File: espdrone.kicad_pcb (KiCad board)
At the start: 6 copper layers, 60 x 60 mm, 503 parts, among them J10 Conn_01x04, J11 Conn_01x04, J12 Conn_01x04, J4 Conn_01x06, J5 Conn_Coaxial, J6 Conn_01x06, J7 Conn_01x06, J8 Conn_01x04, J9 Conn_01x04, Q1 NMOS, Q10 NMOS, Q11 NMOS, Q12 NMOS, Q13 NMOS, Q14 NMOS, Q15 NMOS, Q16 NMOS, Q17 NMOS, Q18 NMOS, Q19 NMOS, Q2 NMOS, Q20 NMOS, Q21 NMOS, Q22 NMOS, Q23 NMOS, Q24 NMOS, Q25 NMOS, Q26 NMOS, Q27 NMOS, Q28 NMOS, Q3 NMOS, Q4 NMOS, Q5 NMOS, Q6 NMOS, Q7 NMOS, Q8 NMOS, Q9 NMOS, U10 FPC-1.0FX-15PWCR-H20, U11 VL53L1CXV0FY1, U12 LIS2MDL, U13 LSM6DS3, U14 PMW3901MB-TXQT_C43496881, U15 STM32G071K8U6, U16 DRV8328ARUYR, U18 STM32G071K8U6, U19 DRV8328ARUYR, U2 USBLC6-2P6, U20 INA180A2, U21 STM32G071K8U6, U22 DRV8328ARUYR, U23 INA180A2, U24 STM32G071K8U6, U25 DRV8328ARUYR, U26 INA180A2, U27 INA190A3IDCKR, U28 INA190A3IDCKR, U29 INA190A3IDCKR, U3 W25Q128JVP, U4 ESP32-C5HF4, U5 LFD182G45DCHD277, U6 TLV62569DBV, U7 INA190A3IDCKR, U8 TPS63070RNMR, U9 TPS2121RUXR, Y1 Crystal_GND24, Y2 Crystal_GND24

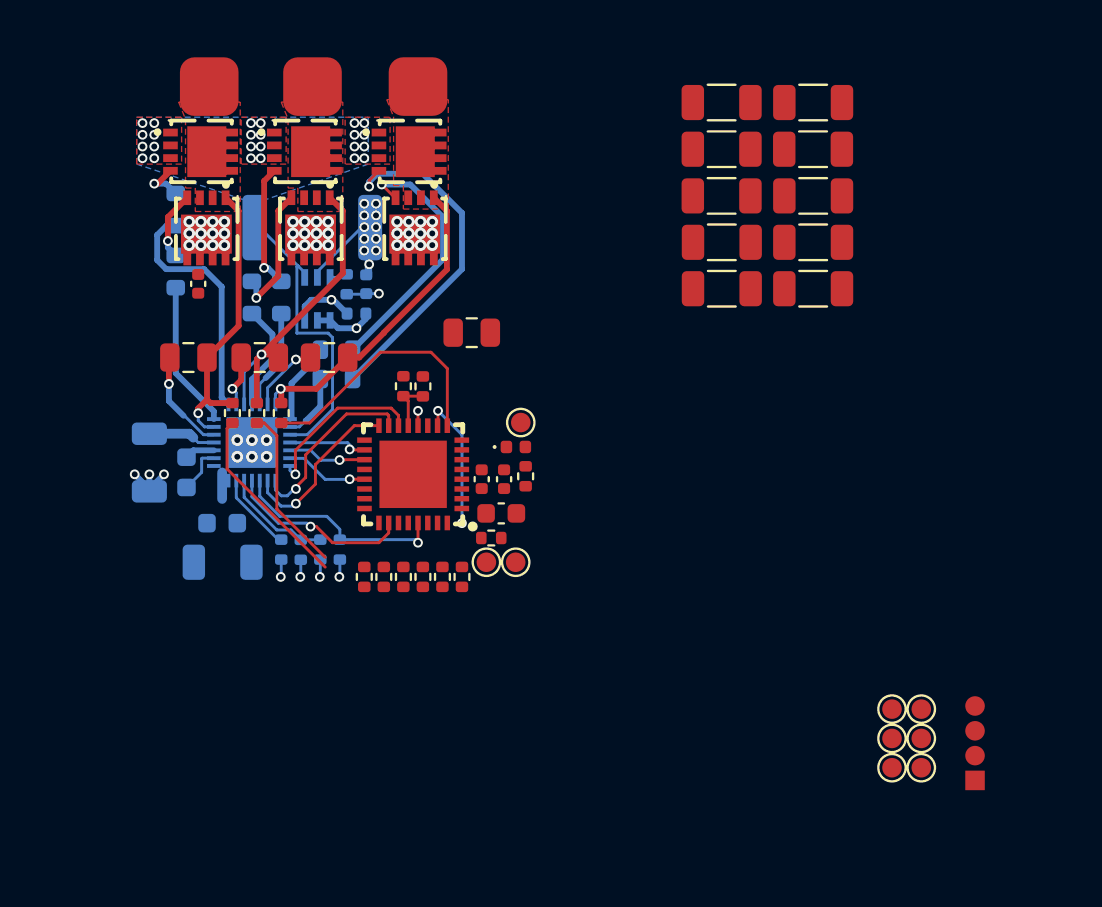
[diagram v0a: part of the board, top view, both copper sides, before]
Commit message: Ostensibly finish ESC routing
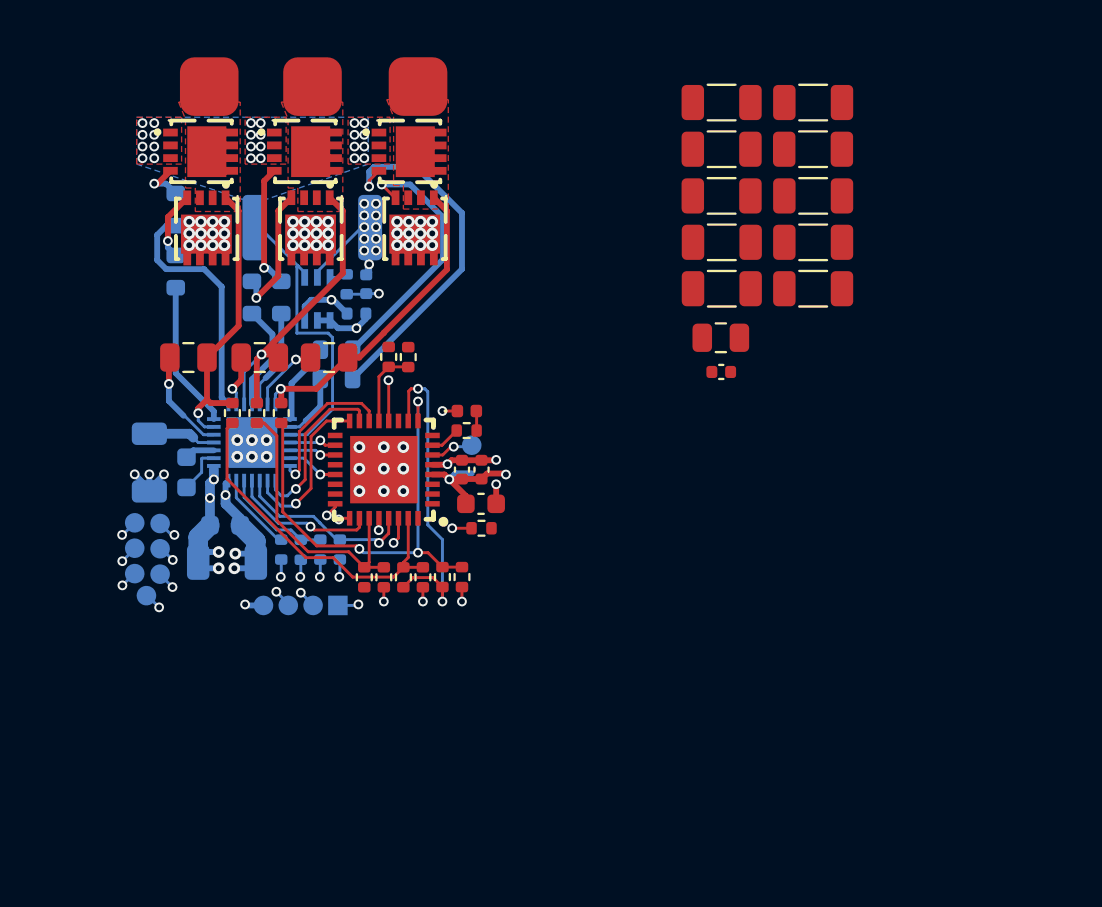
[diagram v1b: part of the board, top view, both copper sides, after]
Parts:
- removed TP19: TestPoint, easyeda2kicad:TestPoint_Pad_D1.0mm_No_Courtyard
- J8, TP11, TP12, TP13, TP14, TP15, TP16, TP17, TP18: moved to B.Cu
- moved TP11 40.2 mm to (116.3, 83.1)
- moved TP12 40.2 mm to (116.3, 81.8)
- moved TP13 40.1 mm to (116.3, 80.5)
- moved TP14 40.0 mm to (115.0, 83.1), turned to 0 degrees
- moved TP15 40.0 mm to (115.0, 81.8), turned to 0 degrees
- moved TP16 39.9 mm to (115.0, 80.5), turned to 0 degrees
- moved J8 33.7 mm to (123.4, 82.5), turned to 0 degrees
- moved C112 27.1 mm to (145.0, 72.8), turned to 180 degrees
- moved TP18 17.5 mm to (115.6, 84.2), turned to 90 degrees
- moved C115 12.8 mm to (145.0, 71.0)
- moved R61 3.82 mm to (132.0, 75.8), turned to 0 degrees
- moved D11 3.11 mm to (132.0, 74.8)
- moved TP17 2.77 mm to (132.2, 76.5), turned to 0 degrees
- moved R75 2.00 mm to (128.8, 83.3)
- moved R76 2.00 mm to (129.8, 83.3)
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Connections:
- TP31 pad 1: /Motors/ESC2/TELEMETRY -> TELEMETRY
- TP43 pad 1: /Motors/ESC3/TELEMETRY -> TELEMETRY
- TP55 pad 1: /Motors/ESC4/TELEMETRY -> TELEMETRY
- U1 pad 6: unconnected-(U1-GPIO6-Pad6) -> TELEMETRY
- U15 pad 30: /Motors/ESC1/TELEMETRY -> TELEMETRY
- U18 pad 30: /Motors/ESC2/TELEMETRY -> TELEMETRY
- U21 pad 30: /Motors/ESC3/TELEMETRY -> TELEMETRY
- U24 pad 30: /Motors/ESC4/TELEMETRY -> TELEMETRY
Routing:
- net GND: track 15.3 -> 31.1 mm, vias 23 -> 43
- net /Motors/ESC1/A_HIGH: track 4.26 -> 17.5 mm, vias 1 -> 2
- net /Motors/ESC1/B_HIGH: track 4.04 -> 15.7 mm, vias 1 -> 2
- net /Motors/ESC1/C_HIGH: track 3.97 -> 15.5 mm, vias 1 -> 2
- net /Motors/ESC1/VSENSE_C: track 13.3 -> 23.7 mm, vias 0 -> 3
- net /Motors/ESC1/VSENSE_REF: track 7.09 -> 16.8 mm
- net /Motors/ESC1/A_LOW: track 8.89 -> 18.1 mm, vias 1 -> 2
- net /Motors/ESC1/NSLEEP: track 9.52 -> 17.9 mm, vias 1 -> 2
- net /Motors/ESC1/VSENSE_A: track 9.57 -> 17.9 mm
- net /Motors/ESC1/B_LOW: track 9.47 -> 17.5 mm, vias 1 -> 2
- net +3V3: track 5.53 -> 13.4 mm, vias 3 -> 6
- net /Motors/ESC1/C_LOW: track 8.67 -> 16.2 mm, vias 1 -> 2
- net /Motors/ESC1/SWDIO: track 0.00 -> 6.78 mm, vias 0 -> 2
- net +BATT: track 1.47 -> 8.12 mm, vias 36 -> 40
- net /Motors/ESC1/VSENSE_B: track 8.55 -> 14.7 mm
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
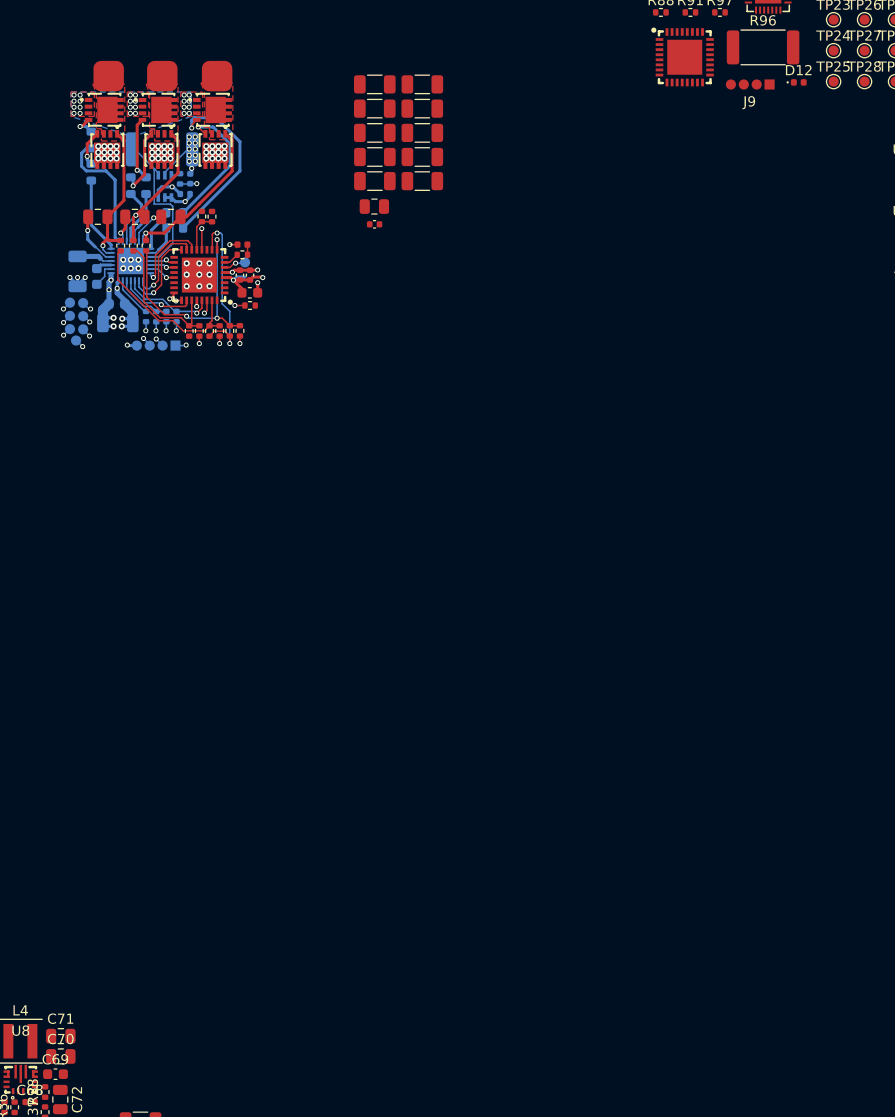
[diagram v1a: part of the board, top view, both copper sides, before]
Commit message: Add dimensions for MOSFET rearranging
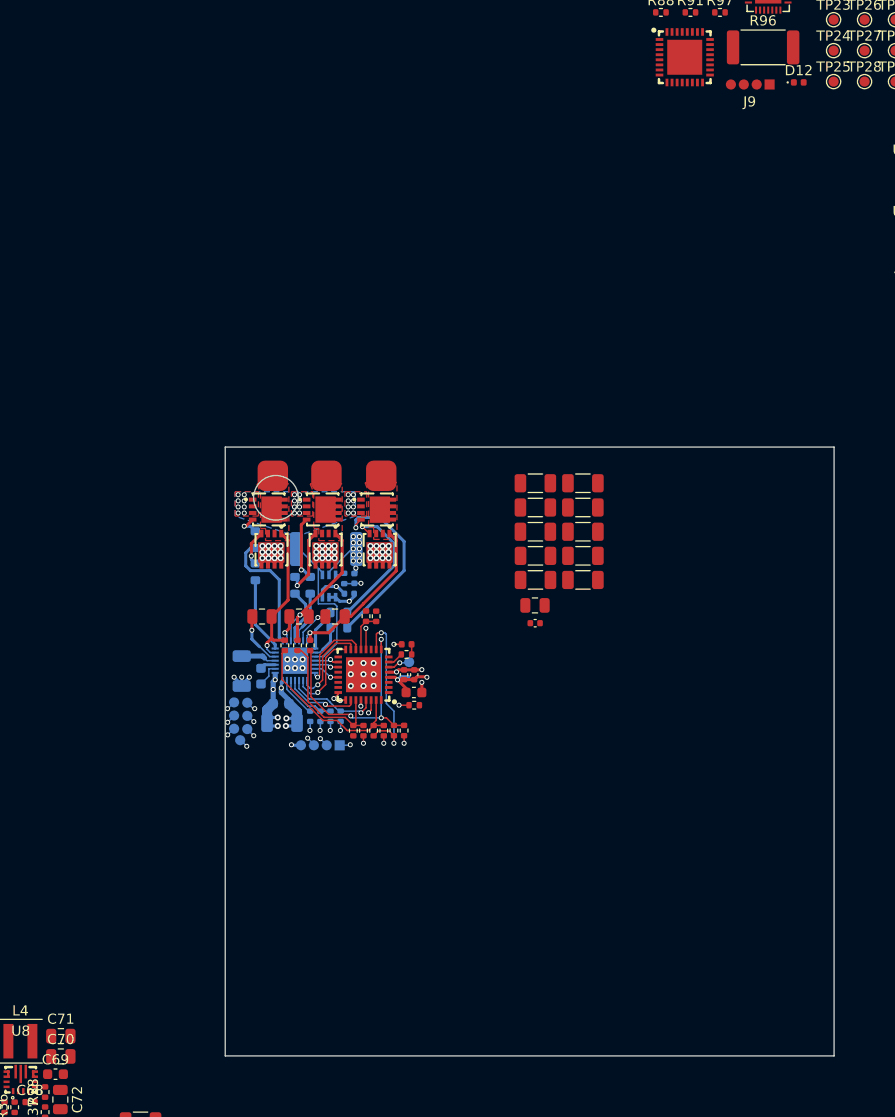
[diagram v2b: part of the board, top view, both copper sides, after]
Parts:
- moved C102 42.6 mm to (135.9, 121.9)
- moved C103 42.6 mm to (135.8, 120.0)
- moved C104 42.6 mm to (148.9, 117.1)
- moved C105 42.6 mm to (131.9, 116.8)
- moved C106 42.6 mm to (147.9, 117.1)
- moved C108 42.6 mm to (148.9, 118.9)
- moved C109 42.6 mm to (133.9, 111.4)
- moved C111 42.6 mm to (141.1, 111.4)
- moved C117 42.6 mm to (142.5, 109.2)
- moved C119 42.6 mm to (143.0, 107.7)
- moved D11 42.6 mm to (148.2, 114.1)
- moved J8 42.6 mm to (139.6, 121.9)
- moved Q7 42.6 mm to (140.2, 104.8)
- moved Q8 42.6 mm to (139.9, 100.9)
- moved R62 42.6 mm to (141.7, 121.2)
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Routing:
- net /Motors/ESC1/B_HIGH: track 15.7 -> 3.34 mm
- net +BATT: track 8.12 -> 20.3 mm
- net GND: track 31.1 -> 35.6 mm
- net /Motors/ESC1/SWCLK: track 6.04 -> 1.49 mm
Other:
- board size 60 x 60 mm -> 167.9 x 121.5 mm

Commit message: Minor ESC adjustments
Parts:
- moved C122 5.53 mm to (155.5, 97.0)
- moved C124 5.53 mm to (155.5, 101.8)
- moved C125 5.53 mm to (155.5, 99.4)
- moved C116 5.53 mm to (155.5, 106.5)
- moved C123 5.53 mm to (155.5, 104.2)
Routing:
- net +BATT: track 20.3 -> 8.12 mm
- net /Motors/ESC1/B_HIGH: track 3.34 -> 13.9 mm
- net GND: track 35.6 -> 31.1 mm
- net /Motors/ESC1/SWCLK: track 1.49 -> 6.04 mm
- net /Motors/ESC1/A_HIGH: track 17.5 -> 14.8 mm
- net /Motors/ESC1/C_HIGH: track 15.7 -> 13.7 mm
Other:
- outline, holes or cut-outs redrawn

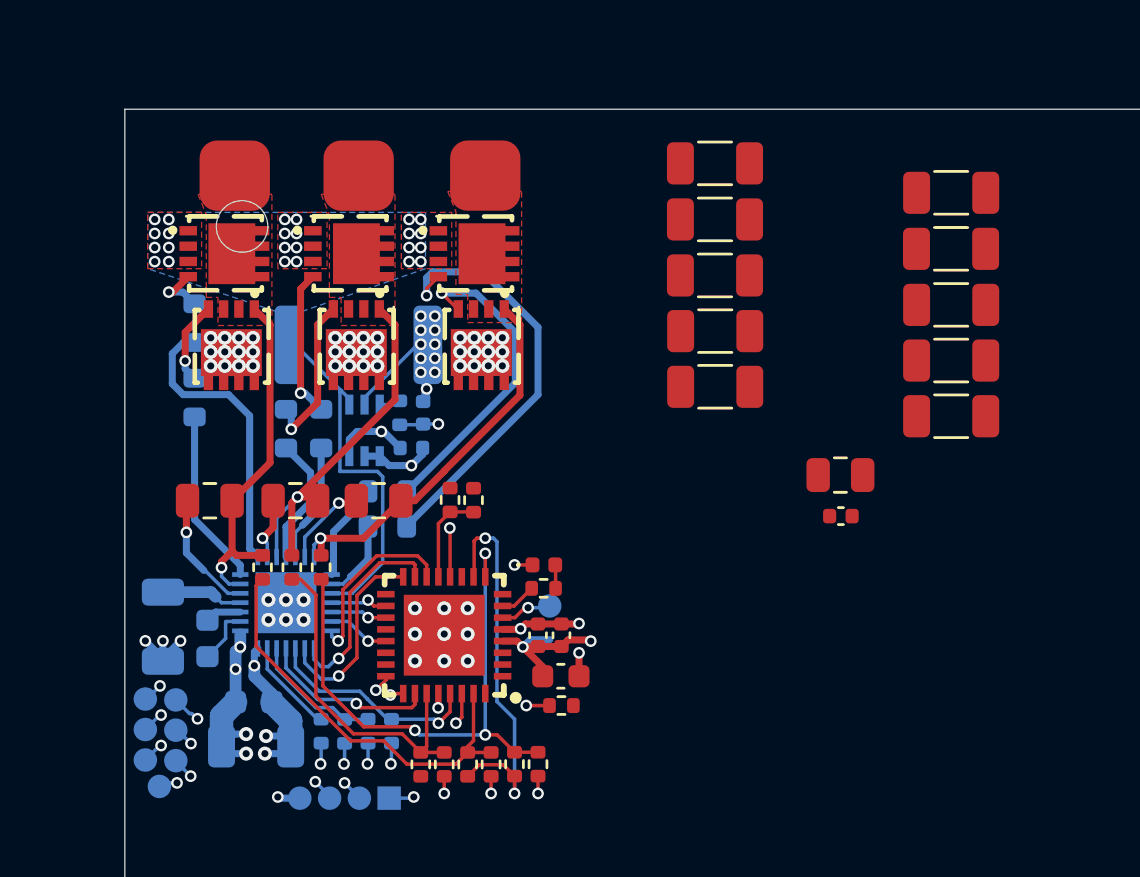
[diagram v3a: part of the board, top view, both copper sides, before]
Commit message: Initial ESC bulk capacitance placement
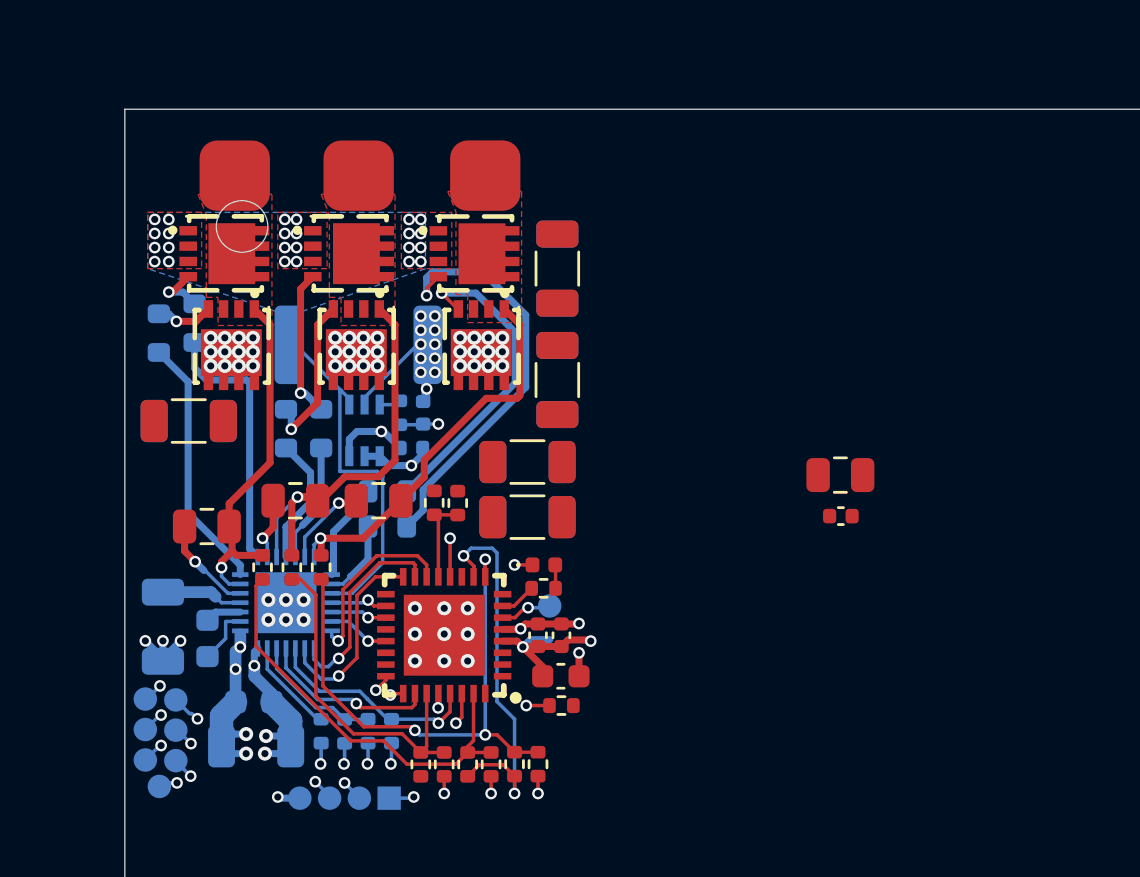
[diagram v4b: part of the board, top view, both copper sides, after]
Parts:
- C113, C114, C118, C120, C121: moved to B.Cu
- moved C114 32.6 mm to (133.0, 108.0)
- moved C116 22.5 mm to (133.0, 108.0), turned to 0 degrees
- moved C120 20.2 mm to (147.5, 109.8)
- moved C121 20.2 mm to (147.5, 112.1)
- moved C118 18.6 mm to (148.8, 106.2), turned to -90 degrees
- moved C113 17.9 mm to (148.8, 101.5), turned to 90 degrees
- moved C124 11.3 mm to (147.5, 109.8), turned to 0 degrees
- moved C123 11.3 mm to (147.5, 112.1), turned to 0 degrees
- moved C125 9.60 mm to (148.8, 106.2), turned to -90 degrees
- moved C122 8.09 mm to (148.8, 101.5), turned to 90 degrees
- moved R69 3.14 mm to (131.8, 104.2)
- moved C109 1.11 mm to (133.8, 112.5)
- moved R67 0.69 mm to (144.5, 111.5)
- moved R68 0.69 mm to (143.5, 111.5)
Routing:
- net /Motors/ESC1/GHA: track 7.53 -> 10.9 mm
- net /Motors/ESC1/PHASE_B: track 16.5 -> 18.0 mm
- net /Motors/ESC1/GLA: track 12.5 -> 11.3 mm
- net /Motors/ESC1/BSTA: track 5.26 -> 4.17 mm
- net Net-(Q5-G): track 3.53 -> 2.47 mm
- net /Motors/ESC1/VSENSE_C: track 23.7 -> 23.2 mm

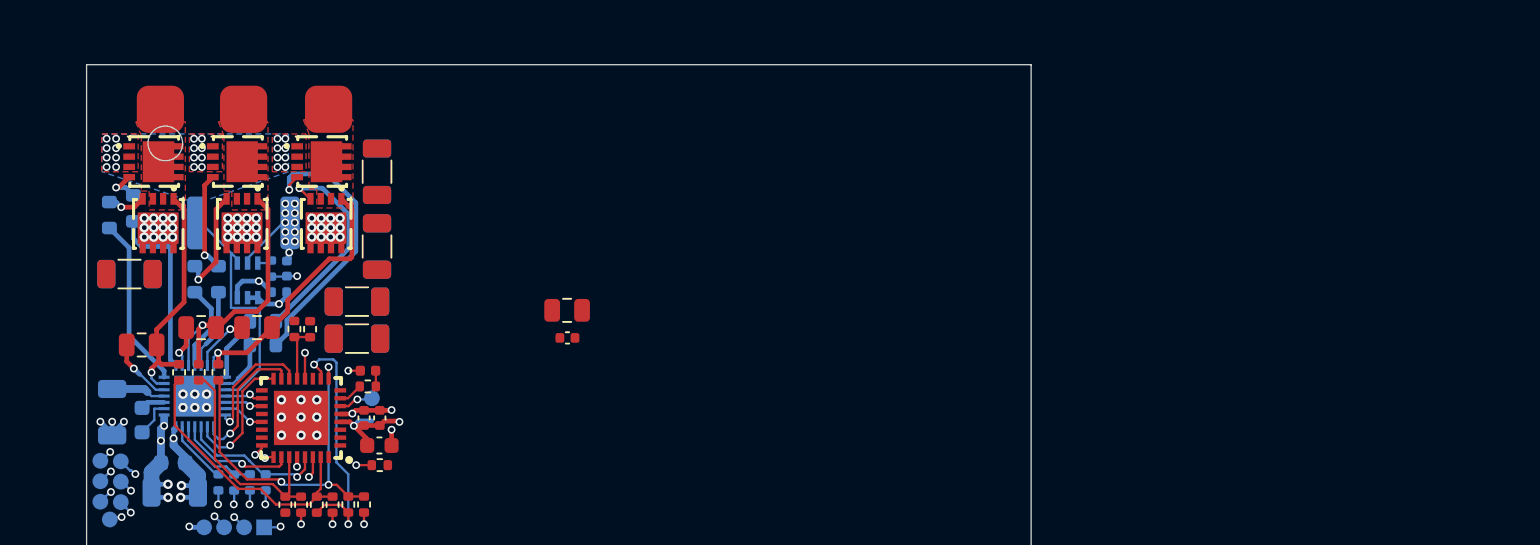
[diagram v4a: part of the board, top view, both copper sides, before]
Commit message: Done routing for first ESC version
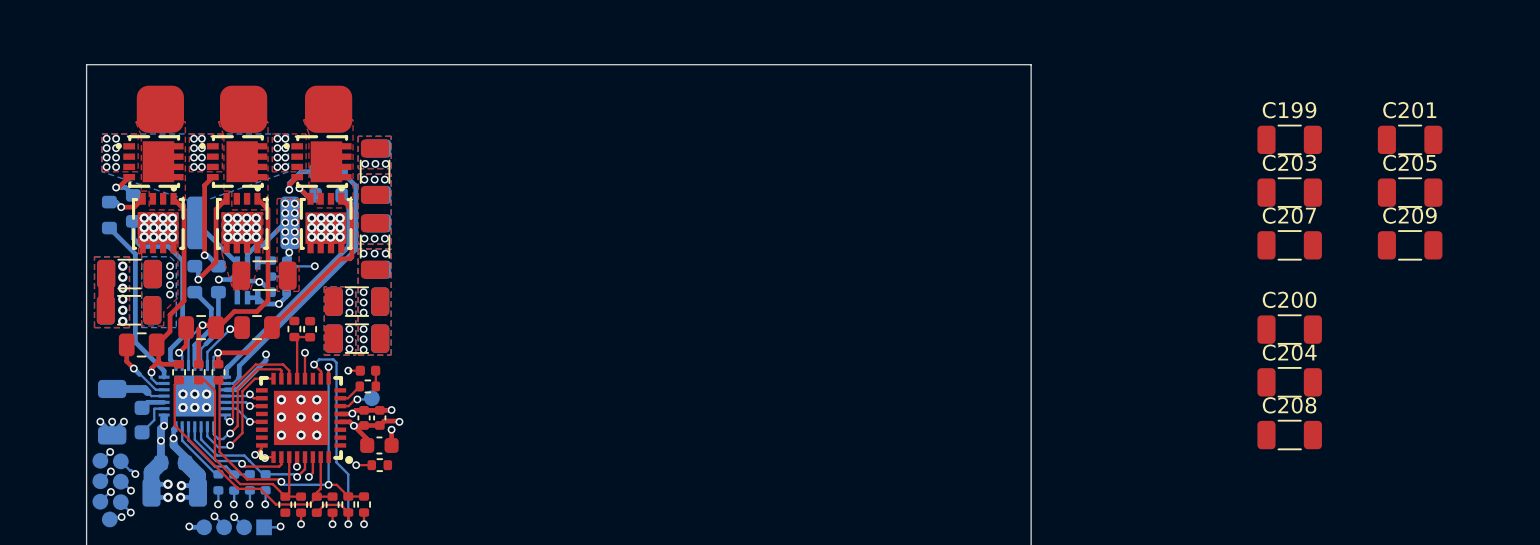
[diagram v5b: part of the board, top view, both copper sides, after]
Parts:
- removed C112: 100n, Capacitor_SMD:C_0402_1005Metric
- removed C115: 1u, Capacitor_SMD:C_0805_2012Metric
- added C198: 10u, Capacitor_SMD:C_1206_3216Metric, F.Cu at (141.6, 108.1)
- added C199: 10u, Capacitor_SMD:C_1206_3216Metric, F.Cu at (206.7, 99.5)
- added C200: 10u, Capacitor_SMD:C_1206_3216Metric, F.Cu at (206.7, 111.5)
- added C201: 10u, Capacitor_SMD:C_1206_3216Metric, F.Cu at (214.4, 99.5)
- added C202: 10u, Capacitor_SMD:C_1206_3216Metric, F.Cu at (133.0, 110.3)
- added C203: 10u, Capacitor_SMD:C_1206_3216Metric, F.Cu at (206.7, 102.8)
- added C204: 10u, Capacitor_SMD:C_1206_3216Metric, F.Cu at (206.7, 114.9)
- added C205: 10u, Capacitor_SMD:C_1206_3216Metric, F.Cu at (214.4, 102.8)
- added C206: 10u, Capacitor_SMD:C_1206_3216Metric, B.Cu at (133.0, 110.3)
- added C207: 10u, Capacitor_SMD:C_1206_3216Metric, F.Cu at (206.7, 106.2)
- added C208: 10u, Capacitor_SMD:C_1206_3216Metric, F.Cu at (206.7, 118.2)
- added C209: 10u, Capacitor_SMD:C_1206_3216Metric, F.Cu at (214.4, 106.2)
- moved R82 11.8 mm to (145.7, 101.5), turned to 0 degrees
- moved R81 9.02 mm to (145.7, 103.0), turned to 0 degrees
- moved C122 0.12 mm to (148.6, 101.5)
- moved C125 0.12 mm to (148.6, 106.2)
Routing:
- net Net-(Q10-G): track 18.0 -> 3.30 mm
- net /Motors/ESC1/GLC: track 3.38 -> 17.5 mm
- net Net-(Q9-G): track 13.5 -> 2.21 mm
- net /Motors/ESC1/GHC: track 4.19 -> 15.0 mm
- net GND: track 31.1 -> 33.7 mm, vias 43 -> 61
- net /Motors/ESC1/ISENSE: track 8.39 -> 10.6 mm
- net +3V3: track 13.4 -> 12.1 mm
- net /Motors/ESC1/GLA: track 11.3 -> 11.9 mm
- net /Motors/ESC1/LSS: track 15.6 -> 15.9 mm, vias 24 -> 26
- net +BATT: vias 40 -> 56
- added copper zone on B.Cu, net +BATT
- added copper zone on F.Cu, net +BATT
- added copper zone on B.Cu, net GND
- added copper zone on F.Cu, net GND
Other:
- outline, holes or cut-outs redrawn
